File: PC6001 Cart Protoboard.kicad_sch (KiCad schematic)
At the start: 19 parts, among them J1 PC-6001 edge connector, SW1 PicoReset, SW2 EspReset, SW3 Button A, U2 ESP32-DevKitC, U3 74LS32, U4 microSD-Breakout, U5 74LS00, U6 SN74LVC245AN, U7 SN74LVC245AN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

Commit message: Release version 1.1
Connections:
- no-connect marks 7 -> 6
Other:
- note removed: "TODO: RAM read/write"
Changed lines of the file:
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@@
-	)
-	(no_connect
-		(at 369.57 104.14)
 	)
 	(no_connect
@@
 		(effects
 			(font
-				(size 1.27 1.27)
-			)
-		)
-	)
-	(text "TODO: RAM read/write"
-		(exclude_from_sim no)
-		(at 77.47 112.395 0)
-		(effects
-			(font

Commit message: Frantically add caps
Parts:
- added C1, C2, C3: 0.1µF, Capacitor_THT:C_Disc_D5.0mm_W2.5mm_P2.50mm, symbol Device:C_Small
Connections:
- net +3.3V: now also C1.1, C2.1, C3.1
- net GND: now also C1.2, C2.2, C3.2

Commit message: Tie address buffer IN/out to always high
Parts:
- added R4: 10kΩ, Resistor_THT:R_Axial_DIN0207_L6.3mm_D2.5mm_P10.16mm_Horizontal, symbol Device:R_Small_US
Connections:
- net +3.3V: now also U7.1 (DIR), U8.1 (DIR), R4.1
- net IN/~{OUT}: now also R4.2; no longer U7.1 (DIR), U8.1 (DIR)
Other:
- note added: "always IN"

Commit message: Pull-up instead of dead short for DIR
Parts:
- added R5, R6: 10kΩ, Resistor_THT:R_Axial_DIN0207_L6.3mm_D2.5mm_P10.16mm_Horizontal, symbol Device:R_Small_US
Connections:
- net +3.3V: now also R5.1, R6.1; no longer U7.1 (DIR), U8.1 (DIR)
- new net: R6.2, U8.1 (DIR)
- new net: R5.2, U7.1 (DIR)
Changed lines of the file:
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@@
 	(wire
 		(pts
-			(xy 100.33 106.68) (xy 108.585 106.68)
+			(xy 83.185 61.595) (xy 83.185 63.5)
 		)
 		(stroke
@@
 	(wire
 		(pts
+			(xy 83.185 101.6) (xy 83.185 106.68)
+		)
+		(stroke
+			(width 0)
+			(type default)
+		)
+	)
+	(wire
+		(pts
 			(xy 191.135 144.78) (xy 191.135 149.86)
 		)
@@
 	(wire
 		(pts
-			(xy 127 154.305) (xy 113.03 154.305)
+			(xy 83.185 71.12) (xy 109.22 71.12)
 		)
 		(stroke
@@
 	(wire
 		(pts
-			(xy 271.78 145.415) (xy 279.4 145.415)
+			(xy 83.185 71.12) (xy 83.185 68.58)
 		)
 		(stroke
@@
 	(wire
 		(pts
-			(xy 86.995 221.615) (xy 86.995 224.155)
+			(xy 83.185 95.885) (xy 83.185 96.52)
 		)
 		(stroke
@@
 	(wire
 		(pts
-			(xy 237.49 78.105) (xy 246.38 78.105)
+			(xy 127 154.305) (xy 113.03 154.305)
 		)
 		(stroke
@@
 	(wire
 		(pts
-			(xy 69.85 208.28) (xy 81.915 208.28)
+			(xy 271.78 145.415) (xy 279.4 145.415)
 		)
 		(stroke
@@
 	(wire
 		(pts
-			(xy 23.495 247.015) (xy 43.815 247.015)
+			(xy 86.995 221.615) (xy 86.995 224.155)
 		)
 		(stroke
@@
 	(wire
 		(pts
-			(xy 318.77 176.53) (xy 326.39 176.53)
+			(xy 237.49 78.105) (xy 246.38 78.105)
+		)
+		(stroke
+			(width 0)
+			(type default)
+		)
+	)
+	(wire
+		(pts
+			(xy 69.85 208.28) (xy 81.915 208.28)
+		)
+		(stroke
+			(width 0)
+			(type default)
+		)
+	)
+	(wire
+		(pts
+			(xy 23.495 247.015) (xy 43.815 247.015)
 		)
 		(stroke
@@
 	(wire
 		(pts
-			(xy 100.965 71.12) (xy 109.22 71.12)
+			(xy 318.77 176.53) (xy 326.39 176.53)
 		)
 		(stroke
@@
 	(wire
 		(pts
+			(xy 83.185 106.68) (xy 108.585 106.68)
+		)
+		(stroke
+			(width 0)
+			(type default)
+		)
+	)
+	(wire
+		(pts
 			(xy 99.695 129.54) (xy 108.585 129.54)
 		)
@@
 	(text "always IN"
 		(exclude_from_sim no)
-		(at 106.68 105.41 0)
+		(at 100.33 105.41 0)
 		(effects
 			(font
@@
 	)
 	(symbol
-		(lib_id "power:+3.3V")
-		(at 100.965 71.12 0)
-		(unit 1)
-		(exclude_from_sim no)
-		(in_bom yes)
-		(on_board yes)
-		(dnp no)
-		(fields_autoplaced yes)
-		(property "Reference" "#PWR025"
-			(at 100.965 74.93 0)
-			(effects
-				(font
-					(size 1.27 1.27)
-				)
-				(hide yes)
-			)
-		)
-		(property "Value" "+3.3V"
-			(at 100.965 66.675 0)
-			(effects
-				(font
-					(size 1.27 1.27)
-				)
-			)
-		)
-		(property "Footprint" ""
-			(at 100.965 71.12 0)
-			(effects
-				(font
-					(size 1.27 1.27)
-				)
-				(hide yes)
-			)
-		)
-		(property "Datasheet" ""
-			(at 100.965 71.12 0)
-			(effects
-				(font
-					(size 1.27 1.27)
-				)
-				(hide yes)
-			)
-		)
-		(property "Description" "Power symbol creates a global label with name \"+3.3V\""
-			(at 100.965 71.12 0)
-			(effects
-				(font
-					(size 1.27 1.27)
-				)
-				(hide yes)
-			)
-		)
-		(pin "1"
-		)
-		(instances
-			(project "PC6001 Cart Protoboard"
-				(path "/43e41326-819e-40e7-9c3a-9c7b5d01c509"
-					(reference "#PWR025")
-					(unit 1)
-				)
-			)
-		)
-	)
-	(symbol
 		(lib_id "74xx:74LS00")
 		(at 27.94 166.37 0)
@@
 	)
 	(symbol
-		(lib_id "power:+3.3V")
-		(at 100.33 106.68 0)
+		(lib_id "Device:R_Small_US")
+		(at 83.185 99.06 0)
 		(unit 1)
 		(exclude_from_sim no)
@@
 		(dnp no)
 		(fields_autoplaced yes)
-		(property "Reference" "#PWR026"
-			(at 100.33 110.49 0)
+		(property "Reference" "R6"
+			(at 85.725 97.7899 0)
 			(effects
 				(font
 					(size 1.27 1.27)
 				)
-				(hide yes)
+				(justify left)
 			)
 		)
-		(property "Value" "+3.3V"
-			(at 100.33 102.235 0)
+		(property "Value" "10kΩ"
+			(at 85.725 100.3299 0)
 			(effects
 				(font
 					(size 1.27 1.27)
 				)
+				(justify left)
 			)
 		)
-		(property "Footprint" ""
-			(at 100.33 106.68 0)
+		(property "Footprint" "Resistor_THT:R_Axial_DIN0207_L6.3mm_D2.5mm_P10.16mm_Horizontal"
+			(at 83.185 99.06 0)
 			(effects
 				(font
@@
 			)
 		)
-		(property "Datasheet" ""
-			(at 100.33 106.68 0)
+		(property "Datasheet" "~"
+			(at 83.185 99.06 0)
 			(effects
 				(font
@@
 			)
 		)
-		(property "Description" "Power symbol creates a global label with name \"+3.3V\""
-			(at 100.33 106.68 0)
+		(property "Description" "Resistor, small US symbol"
+			(at 83.185 99.06 0)
 			(effects
 				(font
@@
 			)
 		)
+		(pin "2"
+		)
 		(pin "1"
 		)
@@
 			(project "PC6001 Cart Protoboard"
 				(path "/43e41326-819e-40e7-9c3a-9c7b5d01c509"
-					(reference "#PWR026")
+					(reference "R6")
 					(unit 1)
 				)
@@
 	)
 	(symbol
+		(lib_id "power:+3.3V")
+		(at 83.185 61.595 0)
+		(unit 1)
+		(exclude_from_sim no)
+		(in_bom yes)
+		(on_board yes)
+		(dnp no)
+		(fields_autoplaced yes)
+		(property "Reference" "#PWR025"
+			(at 83.185 65.405 0)
+			(effects
+				(font
+					(size 1.27 1.27)
+				)
+				(hide yes)
+			)
+		)
+		(property "Value" "+3.3V"
+			(at 83.185 56.515 0)
+			(effects
+				(font
+					(size 1.27 1.27)
+				)
+			)
+		)
+		(property "Footprint" ""
+			(at 83.185 61.595 0)
+			(effects
+				(font
+					(size 1.27 1.27)
+				)
+				(hide yes)
+			)
+		)
+		(property "Datasheet" ""
+			(at 83.185 61.595 0)
+			(effects
+				(font
+					(size 1.27 1.27)
+				)
+				(hide yes)
+			)
+		)
+		(property "Description" "Power symbol creates a global label with name \"+3.3V\""
+			(at 83.185 61.595 0)
+			(effects
+				(font
+					(size 1.27 1.27)
+				)
+				(hide yes)
+			)
+		)
+		(pin "1"
+		)
+		(instances
+			(project ""
+				(path "/43e41326-819e-40e7-9c3a-9c7b5d01c509"
+					(reference "#PWR025")
+					(unit 1)
+				)
+			)
+		)
+	)
+	(symbol
 		(lib_name "GND_3")
 		(lib_id "power:GND")
@@
 					(unit 1)
 				)
+			)
+		)
+	)
+	(symbol
+		(lib_id "power:+3.3V")
+		(at 83.185 95.885 0)
+		(unit 1)
+		(exclude_from_sim no)
+		(in_bom yes)
+		(on_board yes)
+		(dnp no)
+		(fields_autoplaced yes)
+		(property "Reference" "#PWR026"
+			(at 83.185 99.695 0)
+			(effects
+				(font
+					(size 1.27 1.27)
+				)
+				(hide yes)
+			)
+		)
+		(property "Value" "+3.3V"
+			(at 83.185 90.805 0)
+			(effects
+				(font
+					(size 1.27 1.27)
+				)
+			)
+		)
+		(property "Footprint" ""
+			(at 83.185 95.885 0)
+			(effects
+				(font
+					(size 1.27 1.27)
+				)
+				(hide yes)
+			)
+		)
+		(property "Datasheet" ""
+			(at 83.185 95.885 0)
+			(effects
+				(font
+					(size 1.27 1.27)
+				)
+				(hide yes)
+			)
+		)
+		(property "Description" "Power symbol creates a global label with name \"+3.3V\""
+			(at 83.185 95.885 0)
+			(effects
+				(font
+					(size 1.27 1.27)
+				)
+				(hide yes)
+			)
+		)
+		(pin "1"
+		)
+		(instances
+			(project "PC6001 Cart Protoboard"
+				(path "/43e41326-819e-40e7-9c3a-9c7b5d01c509"
+					(reference "#PWR026")
+					(unit 1)
+				)
+			)
+		)
+	)
+	(symbol
+		(lib_id "Device:R_Small_US")
+		(at 83.185 66.04 0)
+		(unit 1)
+		(exclude_from_sim no)
+		(in_bom yes)
+		(on_board yes)
+		(dnp no)
+		(fields_autoplaced yes)
+		(property "Reference" "R5"
+			(at 85.725 64.7699 0)
+			(effects
+				(font
+					(size 1.27 1.27)
+				)
+				(justify left)
+			)
+		)
+		(property "Value" "10kΩ"
+			(at 85.725 67.3099 0)
+			(effects
+				(font
+					(size 1.27 1.27)
+				)
+				(justify left)
+			)
+		)
+		(property "Footprint" "Resistor_THT:R_Axial_DIN0207_L6.3mm_D2.5mm_P10.16mm_Horizontal"
+			(at 83.185 66.04 0)
+			(effects
+				(font
+					(size 1.27 1.27)
+				)
+				(hide yes)
+			)
+		)
+		(property "Datasheet" "~"
+			(at 83.185 66.04 0)
+			(effects
+				(font
+					(size 1.27 1.27)
+				)
+				(hide yes)
+			)
+		)
+		(property "Description" "Resistor, small US symbol"
+			(at 83.185 66.04 0)
+			(effects
+				(font
+					(size 1.27 1.27)
+				)
+				(hide yes)
+			)
+		)
+		(pin "2"
+		)
+		(pin "1"
+		)
+		(instances
+			(project "PC6001 Cart Protoboard"
+				(path "/43e41326-819e-40e7-9c3a-9c7b5d01c509"
+					(reference "R5")
+					(unit 1)
+				)

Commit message: Safety pull-ups routed
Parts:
- R5, R6: value 10kΩ -> 1kΩ
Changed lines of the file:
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@@
 		(fields_autoplaced yes)
 		(property "Reference" "R6"
-			(at 85.725 97.7899 0)
+			(at 85.09 97.7899 0)
 			(effects
 				(font
@@
 			)
 		)
-		(property "Value" "10kΩ"
-			(at 85.725 100.3299 0)
+		(property "Value" "1kΩ"
+			(at 85.09 100.3299 0)
 			(effects
 				(font
@@
 		(fields_autoplaced yes)
 		(property "Reference" "R5"
-			(at 85.725 64.7699 0)
+			(at 85.09 64.7699 0)
 			(effects
 				(font
@@
 			)
 		)
-		(property "Value" "10kΩ"
-			(at 85.725 67.3099 0)
-			(effects
-				(font
+		(property "Value" "1kΩ"
+			(at 85.09 67.3099 0)
+			(effects
+				(font

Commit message: Forcibly route WAIT to GPIO27
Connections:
- net WAIT is gone; now on net ~{WAIT}: J1.7 (Pin_7)
- net ~{WAIT}: now reaches U1.27 (GPIO_24)
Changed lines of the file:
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@@
 		)
 	)
-	(label "WAIT"
+	(label "~{WAIT}"
 		(at 51.435 86.36 180)
 		(fields_autoplaced yes)
@@
 		(fields_autoplaced yes)
 		(effects
+			(font
+				(size 1.27 1.27)
+			)
+			(justify right bottom)
+		)
+	)
+	(label "~{WAIT}"
+		(at 172.085 121.92 180)
+		(fields_autoplaced yes)
+		(effects

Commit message: Ultimate RP2040 is a little longer than we thought
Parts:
- U6: value SN74LVC245AN -> SN74LVC245AN (LoAddr)
- U7: value SN74LVC245AN -> SN74LVC245AN (HiAddr)
- U8: value SN74LVC245AN -> SN74LVC245AN (Data)
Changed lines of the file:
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@@
 		(fields_autoplaced yes)
 		(property "Reference" "U6"
-			(at 121.92 28.575 0)
+			(at 121.92 29.21 0)
 			(effects
 				(font
@@
 			)
 		)
-		(property "Value" "SN74LVC245AN"
-			(at 121.92 31.115 0)
+		(property "Value" "SN74LVC245AN (LoAddr)"
+			(at 121.92 31.75 0)
 			(effects
 				(font
@@
 			)
 		)
-		(property "Value" "SN74LVC245AN"
+		(property "Value" "SN74LVC245AN (HiAddr)"
 			(at 121.92 66.04 0)
 			(effects
@@
 			)
 		)
-		(property "Value" "SN74LVC245AN"
+		(property "Value" "SN74LVC245AN (Data)"
 			(at 121.285 101.6 0)
 			(effects

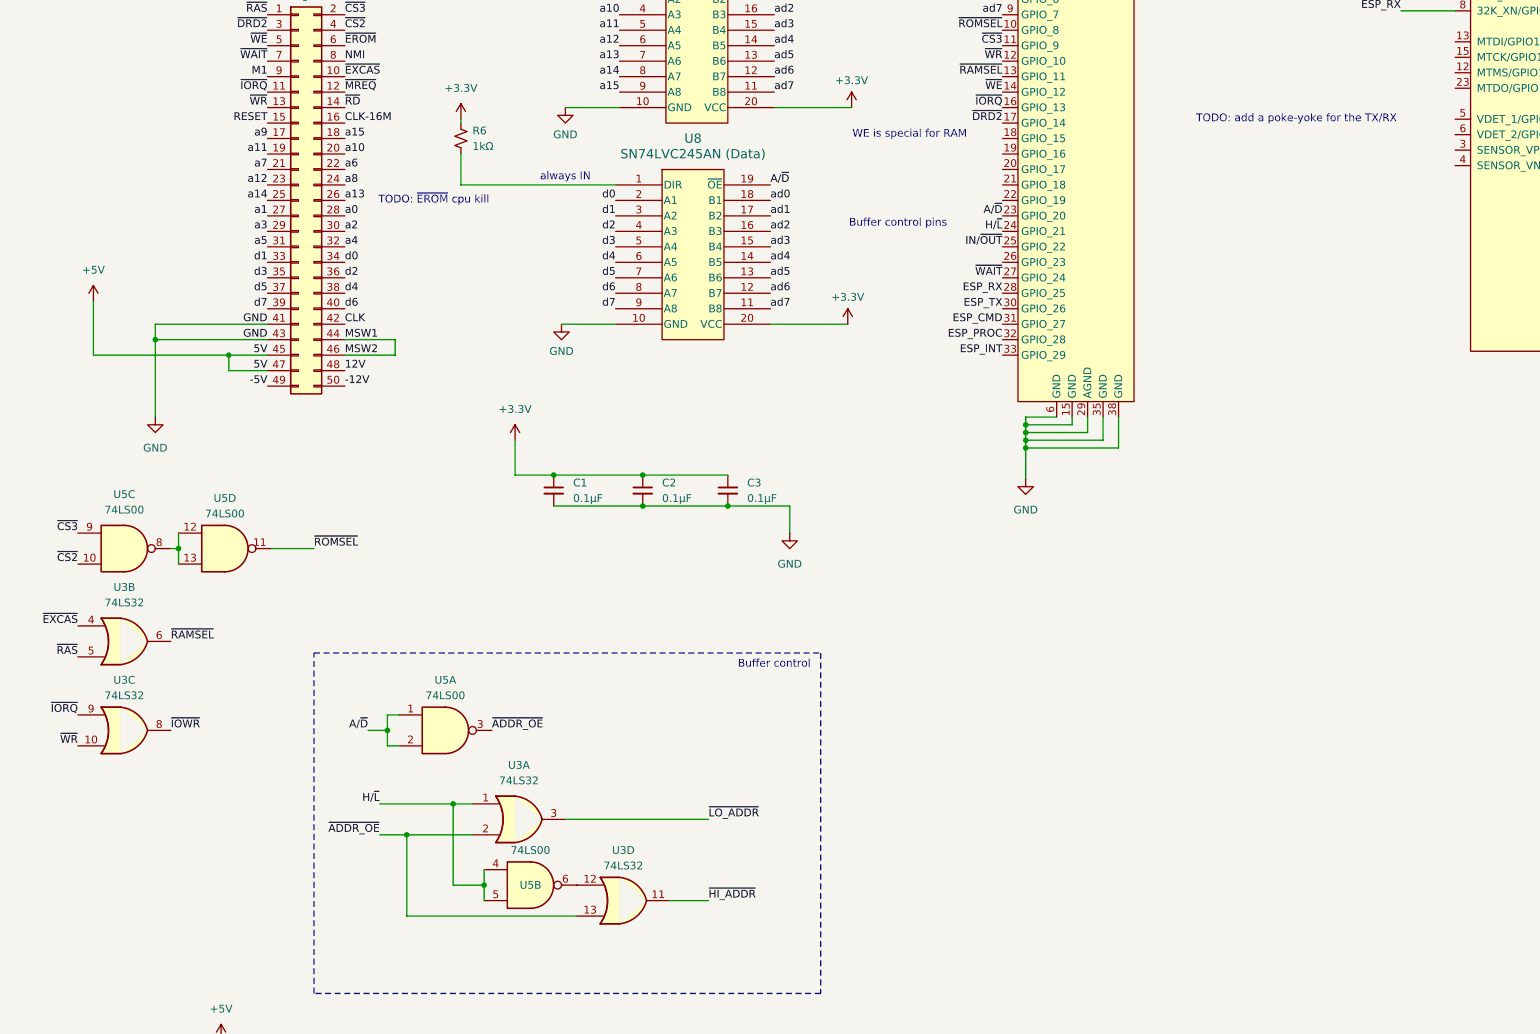
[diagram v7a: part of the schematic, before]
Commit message: Add poka-yoke for RX/TX
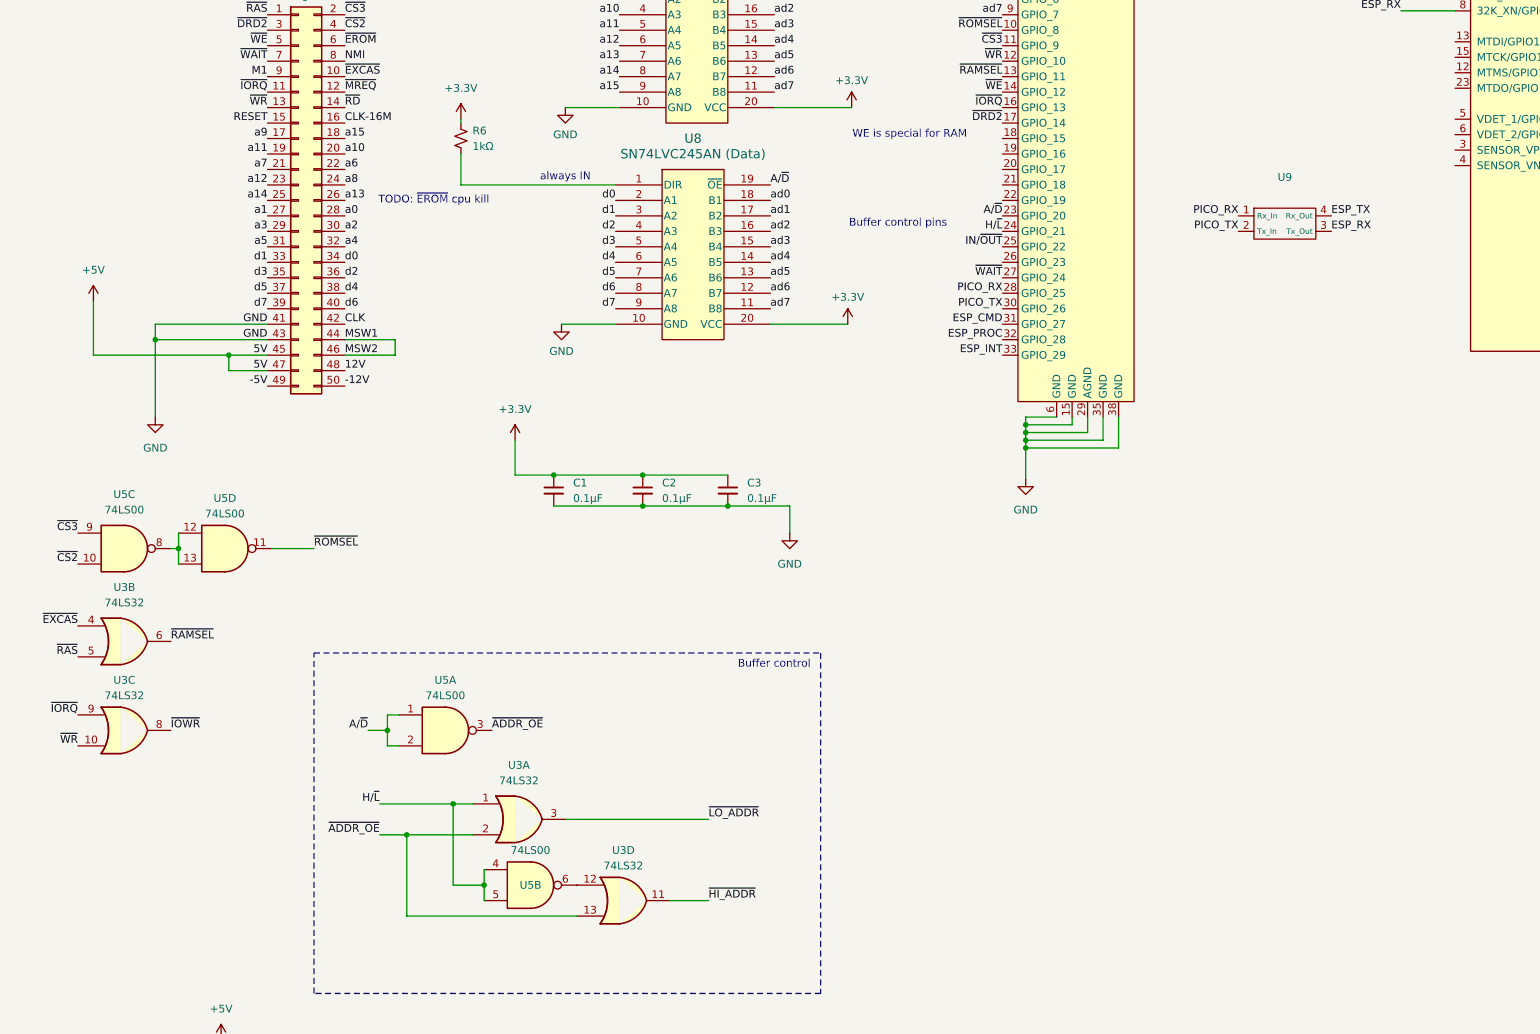
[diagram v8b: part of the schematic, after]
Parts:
- added U9: ~, poka-yoke_rxtx:poka-yoke_rxtx, symbol poka-yoke_rxtx:poka_yoke_txrx
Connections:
- net ESP_RX: now also U9.3 (Tx_Out); no longer U1.28 (GPIO_25)
- net ESP_TX: now also U9.4 (Rx_Out); no longer U1.30 (GPIO_26)
- new net PICO_RX: U1.28 (GPIO_25), U9.1 (Rx_In)
- new net PICO_TX: U1.30 (GPIO_26), U9.2 (Tx_In)
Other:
- note removed: "TODO: add a poke-yoke for the TX/RX"
